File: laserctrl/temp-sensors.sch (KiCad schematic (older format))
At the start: 25 parts, among them P4 CONN_2, P5 CONN_2, P6 CONN_2, P7 CONN_2, Q2 BC807, Q3 BC807

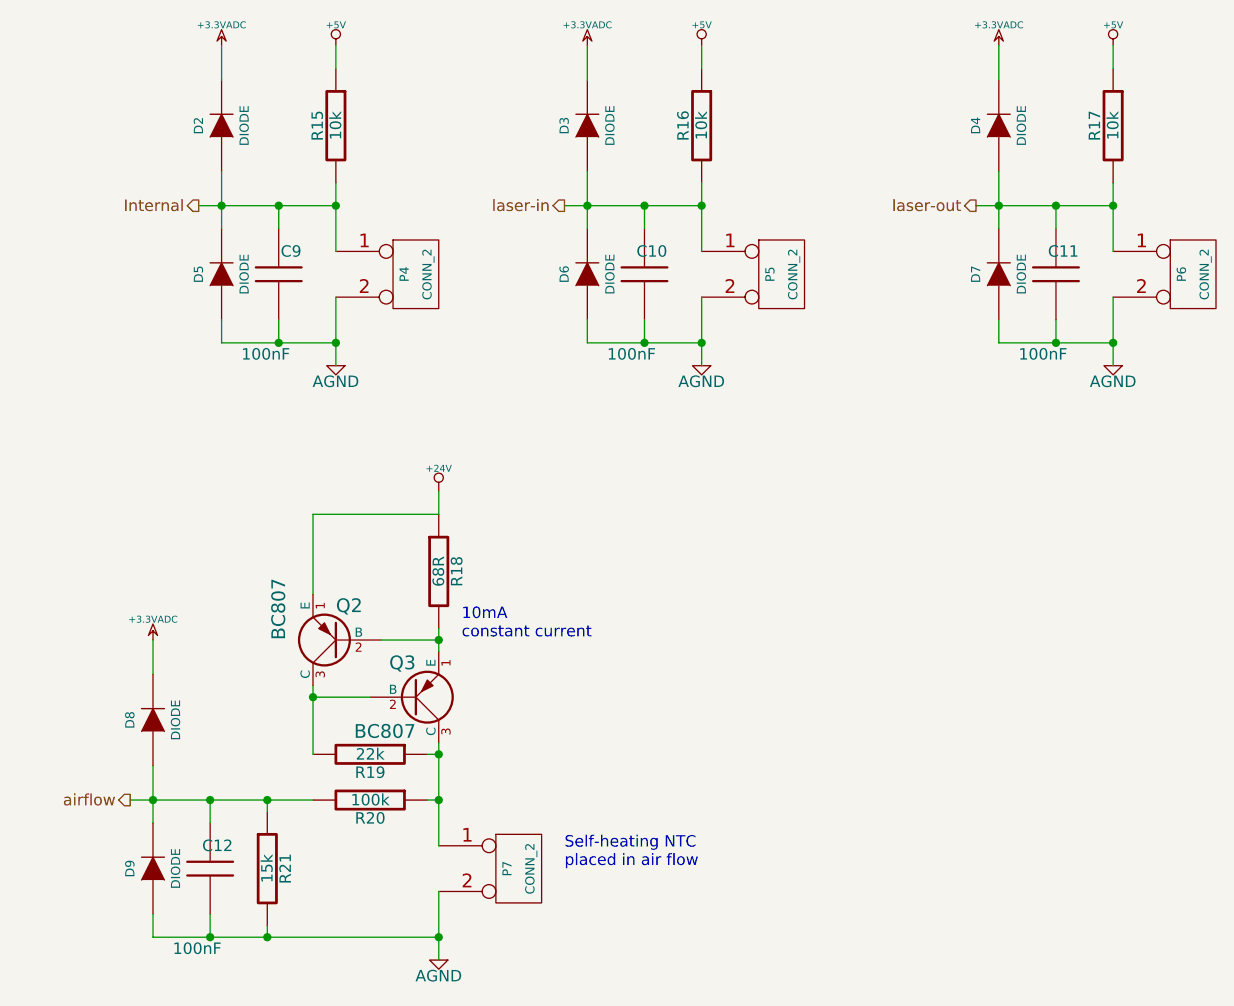
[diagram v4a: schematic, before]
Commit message: Started assigning footprints
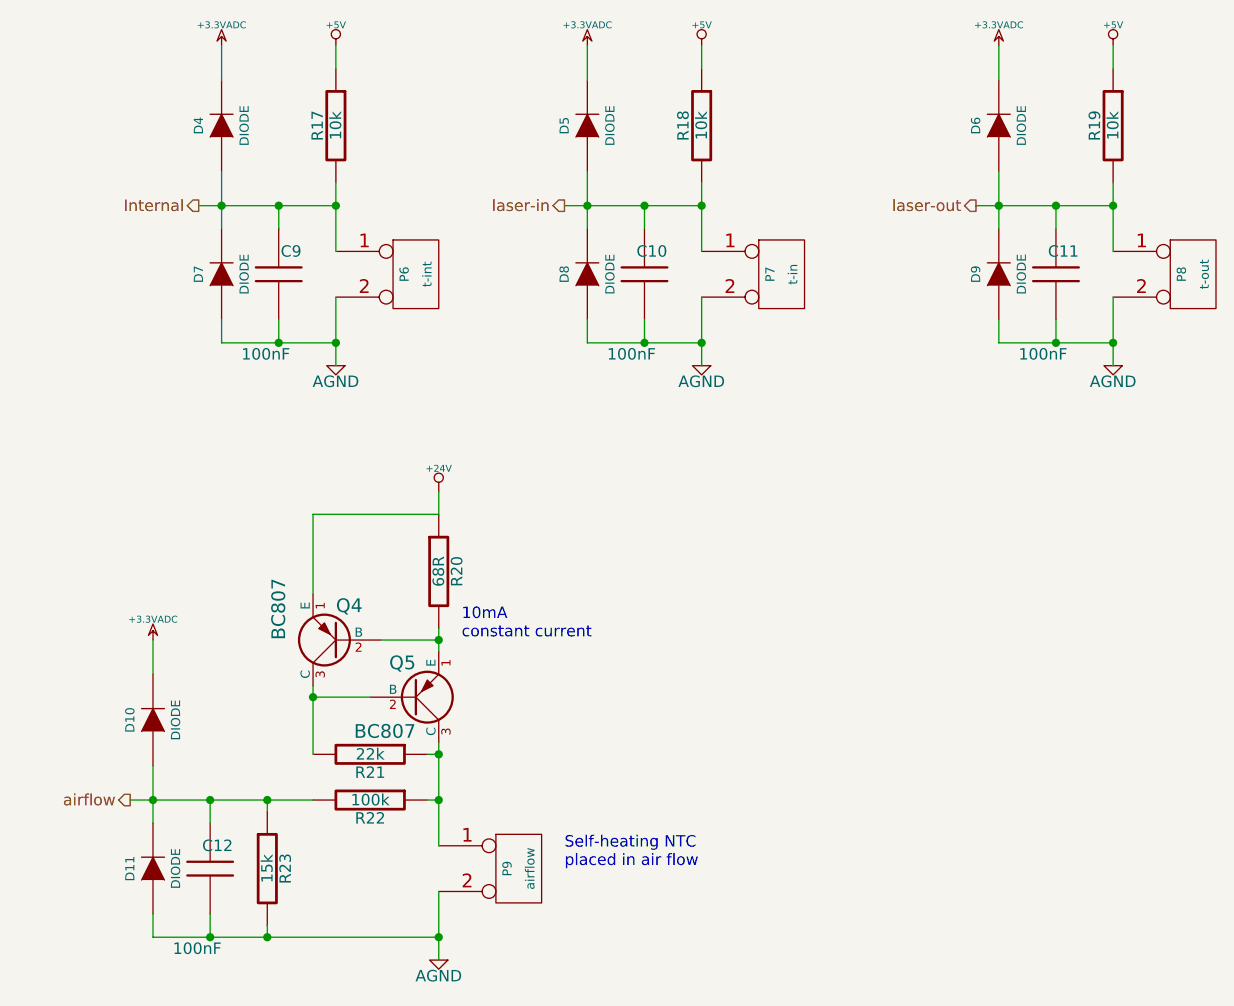
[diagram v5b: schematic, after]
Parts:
- P6: renamed from P4; value CONN_2 -> t-int
- P7: renamed from P5; value CONN_2 -> t-in
- P8: renamed from P6; value CONN_2 -> t-out
- P9: renamed from P7; value CONN_2 -> airflow
- renumbered D8 to D10, D9 to D11, D2 to D4, D3 to D5, D4 to D6, D5 to D7, D6 to D8, D7 to D9, Q2 to Q4, Q3 to Q5, R15 to R17, R16 to R18, R17 to R19, R18 to R20, R19 to R21, R20 to R22, R21 to R23
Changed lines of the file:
@@
-EESchema Schematic File Version 2  date 2011-11-07T21:51:12 CET
+EESchema Schematic File Version 2  date 2011-11-07T23:14:52 CET
 LIBS:power
 LIBS:device
@@
 $Descr A4 11700 8267
 encoding utf-8
-Sheet 4 12
+Sheet 5 12
 Title ""
 Date "7 nov 2011"
@@
 Connection ~ 2000 3950
 $Comp
-L R R19
+L R R21
 U 1 1 4EB5C802
 P 2250 4200
-F 0 "R19" V 2330 4200 50  0000 C CNN
+F 0 "R21" V 2330 4200 50  0000 C CNN
 F 1 "22k" V 2250 4200 50  0000 C CNN
 	1    2250 4200
@@
 10mA\nconstant current
 $Comp
-L +24V #PWR36
+L +24V #PWR031
 U 1 1 4EB542F9
 P 2550 3050
-F 0 "#PWR36" H 2550 3000 20  0001 C CNN
+F 0 "#PWR031" H 2550 3000 20  0001 C CNN
 F 1 "+24V" H 2550 3150 30  0000 C CNN
 	1    2550 3050
@@
 $EndComp
 $Comp
-L R R18
+L R R20
 U 1 1 4EB542D5
 P 2550 3400
-F 0 "R18" V 2630 3400 50  0000 C CNN
+F 0 "R20" V 2630 3400 50  0000 C CNN
 F 1 "68R" V 2550 3400 50  0000 C CNN
 	1    2550 3400
@@
 $EndComp
 $Comp
-L PNP Q2
+L PNP Q4
 U 1 1 4EB542BA
 P 2100 3700
-F 0 "Q2" H 2100 3550 60  0000 R CNN
+F 0 "Q4" H 2100 3550 60  0000 R CNN
 F 1 "BC807" V 2350 3700 60  0000 R CNN
 	1    2100 3700
@@
 $EndComp
 $Comp
-L PNP Q3
+L PNP Q5
 U 1 1 4EB542A8
 P 2450 3950
-F 0 "Q3" H 2450 3800 60  0000 R CNN
+F 0 "Q5" H 2450 3800 60  0000 R CNN
 F 1 "BC807" H 2450 4100 60  0000 R CNN
 	1    2450 3950
@@
 $EndComp
 $Comp
-L R R20
+L R R22
 U 1 1 4EB528F0
 P 2250 4400
-F 0 "R20" V 2330 4400 50  0000 C CNN
+F 0 "R22" V 2330 4400 50  0000 C CNN
 F 1 "100k" V 2250 4400 50  0000 C CNN
 	1    2250 4400
@@
 $EndComp
 $Comp
-L R R21
+L R R23
 U 1 1 4EB528C5
 P 1800 4700
-F 0 "R21" V 1880 4700 50  0000 C CNN
+F 0 "R23" V 1880 4700 50  0000 C CNN
 F 1 "15k" V 1800 4700 50  0000 C CNN
 	1    1800 4700
@@
 $EndComp
 $Comp
-L AGND #PWR38
+L AGND #PWR032
 U 1 1 4EB5260B
 P 2550 5100
-F 0 "#PWR38" H 2550 5100 40  0001 C CNN
+F 0 "#PWR032" H 2550 5100 40  0001 C CNN
 F 1 "AGND" H 2550 5030 50  0000 C CNN
 	1    2550 5100
@@
 airflow
 $Comp
-L CONN_2 P7
+L CONN_2 P9
 U 1 1 4EB5260A
 P 2900 4700
-F 0 "P7" V 2850 4700 40  0000 C CNN
-F 1 "CONN_2" V 2950 4700 40  0000 C CNN
+F 0 "P9" V 2850 4700 40  0000 C CNN
+F 1 "airflow" V 2950 4700 40  0000 C CNN
 	1    2900 4700
 	1    0    0    -1
 $EndComp
 $Comp
-L DIODE D8
+L DIODE D10
 U 1 1 4EB52608
 P 1300 4050
-F 0 "D8" H 1300 4150 40  0000 C CNN
+F 0 "D10" H 1300 4150 40  0000 C CNN
 F 1 "DIODE" H 1300 3950 40  0000 C CNN
 	1    1300 4050
@@
 $EndComp
 $Comp
-L DIODE D9
+L DIODE D11
 U 1 1 4EB52607
 P 1300 4700
-F 0 "D9" H 1300 4800 40  0000 C CNN
+F 0 "D11" H 1300 4800 40  0000 C CNN
 F 1 "DIODE" H 1300 4600 40  0000 C CNN
 	1    1300 4700
@@
 $EndComp
 $Comp
-L +3.3VADC #PWR37
+L +3.3VADC #PWR033
 U 1 1 4EB52606
 P 1300 3700
-F 0 "#PWR37" H 1300 3820 20  0001 C CNN
+F 0 "#PWR033" H 1300 3820 20  0001 C CNN
 F 1 "+3.3VADC" H 1300 3790 30  0000 C CNN
 	1    1300 3700
@@
 $EndComp
 $Comp
-L +3.3VADC #PWR31
+L +3.3VADC #PWR034
 U 1 1 4EB52599
 P 5000 1100
-F 0 "#PWR31" H 5000 1220 20  0001 C CNN
+F 0 "#PWR034" H 5000 1220 20  0001 C CNN
 F 1 "+3.3VADC" H 5000 1190 30  0000 C CNN
 	1    5000 1100
@@
 $EndComp
 $Comp
-L DIODE D7
+L DIODE D9
 U 1 1 4EB52598
 P 5000 2100
-F 0 "D7" H 5000 2200 40  0000 C CNN
+F 0 "D9" H 5000 2200 40  0000 C CNN
 F 1 "DIODE" H 5000 2000 40  0000 C CNN
 	1    5000 2100
@@
 $EndComp
 $Comp
-L DIODE D4
+L DIODE D6
 U 1 1 4EB52597
 P 5000 1450
-F 0 "D4" H 5000 1550 40  0000 C CNN
+F 0 "D6" H 5000 1550 40  0000 C CNN
 F 1 "DIODE" H 5000 1350 40  0000 C CNN
 	1    5000 1450
@@
 $EndComp
 $Comp
-L +5V #PWR32
+L +5V #PWR035
 U 1 1 4EB52596
 P 5500 1100
-F 0 "#PWR32" H 5500 1190 20  0001 C CNN
+F 0 "#PWR035" H 5500 1190 20  0001 C CNN
 F 1 "+5V" H 5500 1190 30  0000 C CNN
 	1    5500 1100
@@
 $EndComp
 $Comp
-L CONN_2 P6
+L CONN_2 P8
 U 1 1 4EB52595
 P 5850 2100
-F 0 "P6" V 5800 2100 40  0000 C CNN
-F 1 "CONN_2" V 5900 2100 40  0000 C CNN
+F 0 "P8" V 5800 2100 40  0000 C CNN
+F 1 "t-out" V 5900 2100 40  0000 C CNN
 	1    5850 2100
 	1    0    0    -1
@@
 laser-out
 $Comp
-L AGND #PWR35
+L AGND #PWR036
 U 1 1 4EB52594
 P 5500 2500
-F 0 "#PWR35" H 5500 2500 40  0001 C CNN
+F 0 "#PWR036" H 5500 2500 40  0001 C CNN
 F 1 "AGND" H 5500 2430 50  0000 C CNN
 	1    5500 2500
@@
 $EndComp
 $Comp
-L R R17
+L R R19
 U 1 1 4EB52592
 P 5500 1450
-F 0 "R17" V 5580 1450 50  0000 C CNN
+F 0 "R19" V 5580 1450 50  0000 C CNN
 F 1 "10k" V 5500 1450 50  0000 C CNN
 	1    5500 1450
@@
 $EndComp
 $Comp
-L R R16
+L R R18
 U 1 1 4EB52540
 P 3700 1450
-F 0 "R16" V 3780 1450 50  0000 C CNN
+F 0 "R18" V 3780 1450 50  0000 C CNN
 F 1 "10k" V 3700 1450 50  0000 C CNN
 	1    3700 1450
@@
 $EndComp
 $Comp
-L AGND #PWR34
+L AGND #PWR037
 U 1 1 4EB5253E
 P 3700 2500
-F 0 "#PWR34" H 3700 2500 40  0001 C CNN
+F 0 "#PWR037" H 3700 2500 40  0001 C CNN
 F 1 "AGND" H 3700 2430 50  0000 C CNN
 	1    3700 2500
@@
 laser-in
 $Comp
-L CONN_2 P5
+L CONN_2 P7
 U 1 1 4EB5253D
 P 4050 2100
-F 0 "P5" V 4000 2100 40  0000 C CNN
-F 1 "CONN_2" V 4100 2100 40  0000 C CNN
+F 0 "P7" V 4000 2100 40  0000 C CNN
+F 1 "t-in" V 4100 2100 40  0000 C CNN
 	1    4050 2100
 	1    0    0    -1
 $EndComp
 $Comp
-L +5V #PWR30
+L +5V #PWR038
 U 1 1 4EB5253C
 P 3700 1100
-F 0 "#PWR30" H 3700 1190 20  0001 C CNN
+F 0 "#PWR038" H 3700 1190 20  0001 C CNN
 F 1 "+5V" H 3700 1190 30  0000 C CNN
 	1    3700 1100
@@
 $EndComp
 $Comp
-L DIODE D3
+L DIODE D5
 U 1 1 4EB5253B
 P 3200 1450
-F 0 "D3" H 3200 1550 40  0000 C CNN
+F 0 "D5" H 3200 1550 40  0000 C CNN
 F 1 "DIODE" H 3200 1350 40  0000 C CNN
 	1    3200 1450
@@
 $EndComp
 $Comp
-L DIODE D6
+L DIODE D8
 U 1 1 4EB5253A
 P 3200 2100
-F 0 "D6" H 3200 2200 40  0000 C CNN
+F 0 "D8" H 3200 2200 40  0000 C CNN
 F 1 "DIODE" H 3200 2000 40  0000 C CNN
 	1    3200 2100
@@
 $EndComp
 $Comp
-L +3.3VADC #PWR29
+L +3.3VADC #PWR039
 U 1 1 4EB52539
 P 3200 1100
-F 0 "#PWR29" H 3200 1220 20  0001 C CNN
+F 0 "#PWR039" H 3200 1220 20  0001 C CNN
 F 1 "+3.3VADC" H 3200 1190 30  0000 C CNN
 	1    3200 1100
@@
 $EndComp
 $Comp
-L +3.3VADC #PWR27
+L +3.3VADC #PWR040
 U 1 1 4EB52427
 P 1600 1100
-F 0 "#PWR27" H 1600 1220 20  0001 C CNN
+F 0 "#PWR040" H 1600 1220 20  0001 C CNN
 F 1 "+3.3VADC" H 1600 1190 30  0000 C CNN
 	1    1600 1100
@@
 $EndComp
 $Comp
-L DIODE D5
+L DIODE D7
 U 1 1 4EB52405
 P 1600 2100
-F 0 "D5" H 1600 2200 40  0000 C CNN
+F 0 "D7" H 1600 2200 40  0000 C CNN
 F 1 "DIODE" H 1600 2000 40  0000 C CNN
 	1    1600 2100
@@
 $EndComp
 $Comp
-L DIODE D2
+L DIODE D4
 U 1 1 4EB523F4
 P 1600 1450
-F 0 "D2" H 1600 1550 40  0000 C CNN
+F 0 "D4" H 1600 1550 40  0000 C CNN
 F 1 "DIODE" H 1600 1350 40  0000 C CNN
 	1    1600 1450
@@
 $EndComp
 $Comp
-L +5V #PWR28
+L +5V #PWR041
 U 1 1 4EB523C5
 P 2100 1100
-F 0 "#PWR28" H 2100 1190 20  0001 C CNN
+F 0 "#PWR041" H 2100 1190 20  0001 C CNN
 F 1 "+5V" H 2100 1190 30  0000 C CNN
 	1    2100 1100
@@
 $EndComp
 $Comp
-L CONN_2 P4
+L CONN_2 P6
 U 1 1 4EB523A3
 P 2450 2100
-F 0 "P4" V 2400 2100 40  0000 C CNN
-F 1 "CONN_2" V 2500 2100 40  0000 C CNN
+F 0 "P6" V 2400 2100 40  0000 C CNN
+F 1 "t-int" V 2500 2100 40  0000 C CNN
 	1    2450 2100
 	1    0    0    -1
@@
 Internal
 $Comp
-L AGND #PWR33
+L AGND #PWR042
 U 1 1 4EB472F1
 P 2100 2500
-F 0 "#PWR33" H 2100 2500 40  0001 C CNN
+F 0 "#PWR042" H 2100 2500 40  0001 C CNN
 F 1 "AGND" H 2100 2430 50  0000 C CNN
 	1    2100 2500
@@
 $EndComp
 $Comp
-L R R15
+L R R17
 U 1 1 4EB46A84
 P 2100 1450
-F 0 "R15" V 2180 1450 50  0000 C CNN
+F 0 "R17" V 2180 1450 50  0000 C CNN
 F 1 "10k" V 2100 1450 50  0000 C CNN
 	1    2100 1450

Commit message: Use double-shottky diodes in stead of tons of discrete miniMELFs
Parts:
- removed D10, D11, D4, D5, D6, D7, D8, D9: DIODE, symbol DIODE
- added D3, D4, D5, D6: BAT 54S, symbol DIODE2
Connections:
- wire segments 50 -> 46
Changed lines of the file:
@@
-EESchema Schematic File Version 2  date 2011-11-09T19:37:00 CET
+EESchema Schematic File Version 2  date 2011-11-09T22:36:32 CET
 LIBS:power
 LIBS:device
@@
 LIBS:microsd
 LIBS:jumper3
+LIBS:diode2
+LIBS:laserctrl-cache
 EELAYER 25  0
 EELAYER END
@@
 Comment4 ""
 $EndDescr
+Wire Wire Line
+	1300 4100 1300 3700
+Wire Wire Line
+	2000 4400 1200 4400
+Connection ~ 1300 4400
+Wire Wire Line
+	5000 2100 5000 2400
+Wire Wire Line
+	5000 2400 5500 2400
+Wire Wire Line
+	4900 1800 5500 1800
+Connection ~ 5000 1800
+Wire Wire Line
+	5000 1500 5000 1100
+Wire Wire Line
+	3200 2100 3200 2400
+Wire Wire Line
+	3200 2400 3700 2400
+Wire Wire Line
+	3100 1800 3700 1800
+Connection ~ 3200 1800
+Wire Wire Line
+	3200 1500 3200 1100
+Wire Wire Line
+	1600 1500 1600 1100
 Connection ~ 2550 4200
 Wire Wire Line
@@
 Wire Wire Line
 	2500 4400 2550 4400
-Wire Wire Line
-	1600 1100 1600 1250
 Connection ~ 1600 1800
 Wire Wire Line
@@
 Connection ~ 2100 2400
 Wire Wire Line
-	1600 2300 1600 2400
-Wire Wire Line
-	1600 2400 2100 2400
+	2100 2400 1600 2400
 Connection ~ 1850 2400
-Wire Wire Line
-	1600 1900 1600 1650
-Wire Wire Line
-	3200 1900 3200 1650
 Connection ~ 3450 2400
-Wire Wire Line
-	3700 2400 3200 2400
-Wire Wire Line
-	3200 2400 3200 2300
 Connection ~ 3700 2400
 Wire Wire Line
@@
 Connection ~ 3700 1800
 Wire Wire Line
-	3100 1800 3700 1800
-Wire Wire Line
 	3450 2400 3450 2300
 Wire Wire Line
@@
 Wire Wire Line
 	3700 1100 3700 1200
-Connection ~ 3200 1800
-Wire Wire Line
-	3200 1100 3200 1250
-Wire Wire Line
-	5000 1100 5000 1250
-Connection ~ 5000 1800
 Wire Wire Line
 	5500 1100 5500 1200
@@
 Wire Wire Line
 	5250 2300 5250 2400
-Wire Wire Line
-	4900 1800 5500 1800
 Connection ~ 5500 1800
 Wire Wire Line
 	5500 2500 5500 2200
 Connection ~ 5500 2400
-Wire Wire Line
-	5000 2300 5000 2400
-Wire Wire Line
-	5000 2400 5500 2400
 Connection ~ 5250 2400
-Wire Wire Line
-	5000 1900 5000 1650
-Wire Wire Line
-	1300 4500 1300 4250
 Connection ~ 1550 5000
-Wire Wire Line
-	1300 4900 1300 5000
 Connection ~ 2550 5000
 Wire Wire Line
@@
 	1550 4400 1550 4500
 Connection ~ 1550 4400
-Connection ~ 1300 4400
-Wire Wire Line
-	1300 3700 1300 3850
-Wire Wire Line
-	1200 4400 2000 4400
-Wire Wire Line
-	1300 5000 2550 5000
+Wire Wire Line
+	2550 5000 1300 5000
 Wire Wire Line
 	2550 3150 2550 3050
@@
 	2000 3900 2000 4200
 Connection ~ 2000 3950
+Wire Wire Line
+	1600 2400 1600 2100
+Wire Wire Line
+	1300 5000 1300 4700
+$Comp
+L DIODE2 D6
+U 1 1 4EBAE319
+P 1300 4400
+F 0 "D6" H 1450 4500 60  0000 C CNN
+F 1 "BAT 54S" H 1550 4600 60  0000 C CNN
+	1    1300 4400
+	-1   0    0    1
+$EndComp
+$Comp
+L +3.3VADC #PWR030
+U 1 1 4EBAE2EF
+P 5000 1100
+F 0 "#PWR030" H 5000 1220 20  0001 C CNN
+F 1 "+3.3VADC" H 5000 1190 30  0000 C CNN
+	1    5000 1100
+	1    0    0    -1
+$EndComp
+$Comp
+L DIODE2 D5
+U 1 1 4EBAE2EE
+P 5000 1800
+F 0 "D5" H 5150 1900 60  0000 C CNN
+F 1 "BAT 54S" H 5250 2000 60  0000 C CNN
+	1    5000 1800
+	-1   0    0    1
+$EndComp
+$Comp
+L +3.3VADC #PWR031
+U 1 1 4EBAE2E3
+P 3200 1100
+F 0 "#PWR031" H 3200 1220 20  0001 C CNN
+F 1 "+3.3VADC" H 3200 1190 30  0000 C CNN
+	1    3200 1100
+	1    0    0    -1
+$EndComp
+$Comp
+L DIODE2 D4
+U 1 1 4EBAE2E2
+P 3200 1800
+F 0 "D4" H 3350 1900 60  0000 C CNN
+F 1 "BAT 54S" H 3450 2000 60  0000 C CNN
+	1    3200 1800
+	-1   0    0    1
+$EndComp
+$Comp
+L DIODE2 D3
+U 1 1 4EBAE288
+P 1600 1800
+F 0 "D3" H 1750 1900 60  0000 C CNN
+F 1 "BAT 54S" H 1850 2000 60  0000 C CNN
+	1    1600 1800
+	-1   0    0    1
+$EndComp
 $Comp
 L R R21
@@
 10mA\nconstant current
 $Comp
-L +24V #PWR39
+L +24V #PWR032
 U 1 1 4EB542F9
 P 2550 3050
-F 0 "#PWR39" H 2550 3000 20  0001 C CNN
+F 0 "#PWR032" H 2550 3000 20  0001 C CNN
 F 1 "+24V" H 2550 3150 30  0000 C CNN
 	1    2550 3050
@@
 $EndComp
 $Comp
-L AGND #PWR41
+L AGND #PWR033
 U 1 1 4EB5260B
 P 2550 5100
-F 0 "#PWR41" H 2550 5100 40  0001 C CNN
+F 0 "#PWR033" H 2550 5100 40  0001 C CNN
 F 1 "AGND" H 2550 5030 50  0000 C CNN
 	1    2550 5100
@@
 $EndComp
 $Comp
-L DIODE D10
-U 1 1 4EB52608
-P 1300 4050
-F 0 "D10" H 1300 4150 40  0000 C CNN
-F 1 "DIODE" H 1300 3950 40  0000 C CNN
-	1    1300 4050
-	0    -1   -1   0
-$EndComp
-$Comp
-L DIODE D11
-U 1 1 4EB52607
-P 1300 4700
-F 0 "D11" H 1300 4800 40  0000 C CNN
-F 1 "DIODE" H 1300 4600 40  0000 C CNN
-	1    1300 4700
-	0    -1   -1   0
-$EndComp
-$Comp
-L +3.3VADC #PWR40
+L +3.3VADC #PWR034
 U 1 1 4EB52606
 P 1300 3700
-F 0 "#PWR40" H 1300 3820 20  0001 C CNN
+F 0 "#PWR034" H 1300 3820 20  0001 C CNN
 F 1 "+3.3VADC" H 1300 3790 30  0000 C CNN
 	1    1300 3700
@@
 $EndComp
 $Comp
-L +3.3VADC #PWR34
-U 1 1 4EB52599
-P 5000 1100
-F 0 "#PWR34" H 5000 1220 20  0001 C CNN
-F 1 "+3.3VADC" H 5000 1190 30  0000 C CNN
-	1    5000 1100
-	1    0    0    -1
-$EndComp
-$Comp
-L DIODE D9
-U 1 1 4EB52598
-P 5000 2100
-F 0 "D9" H 5000 2200 40  0000 C CNN
-F 1 "DIODE" H 5000 2000 40  0000 C CNN
-	1    5000 2100
-	0    -1   -1   0
-$EndComp
-$Comp
-L DIODE D6
-U 1 1 4EB52597
-P 5000 1450
-F 0 "D6" H 5000 1550 40  0000 C CNN
-F 1 "DIODE" H 5000 1350 40  0000 C CNN
-	1    5000 1450
-	0    -1   -1   0
-$EndComp
-$Comp
-L +5V #PWR35
+L +5V #PWR035
 U 1 1 4EB52596
 P 5500 1100
-F 0 "#PWR35" H 5500 1190 20  0001 C CNN
+F 0 "#PWR035" H 5500 1190 20  0001 C CNN
 F 1 "+5V" H 5500 1190 30  0000 C CNN
 	1    5500 1100
@@
 laser-out
 $Comp
-L AGND #PWR38
+L AGND #PWR036
 U 1 1 4EB52594
 P 5500 2500
-F 0 "#PWR38" H 5500 2500 40  0001 C CNN
+F 0 "#PWR036" H 5500 2500 40  0001 C CNN
 F 1 "AGND" H 5500 2430 50  0000 C CNN
 	1    5500 2500
@@
 $EndComp
 $Comp
-L AGND #PWR37
+L AGND #PWR037
 U 1 1 4EB5253E
 P 3700 2500
-F 0 "#PWR37" H 3700 2500 40  0001 C CNN
+F 0 "#PWR037" H 3700 2500 40  0001 C CNN
 F 1 "AGND" H 3700 2430 50  0000 C CNN
 	1    3700 2500
@@
 $EndComp
 $Comp
-L +5V #PWR33
+L +5V #PWR038
 U 1 1 4EB5253C
 P 3700 1100
-F 0 "#PWR33" H 3700 1190 20  0001 C CNN
+F 0 "#PWR038" H 3700 1190 20  0001 C CNN
 F 1 "+5V" H 3700 1190 30  0000 C CNN
 	1    3700 1100
@@
 $EndComp
 $Comp
-L DIODE D5
-U 1 1 4EB5253B
-P 3200 1450
-F 0 "D5" H 3200 1550 40  0000 C CNN
-F 1 "DIODE" H 3200 1350 40  0000 C CNN
-	1    3200 1450
-	0    -1   -1   0
-$EndComp
-$Comp
-L DIODE D8
-U 1 1 4EB5253A
-P 3200 2100
-F 0 "D8" H 3200 2200 40  0000 C CNN
-F 1 "DIODE" H 3200 2000 40  0000 C CNN
-	1    3200 2100
-	0    -1   -1   0
-$EndComp
-$Comp
-L +3.3VADC #PWR32
-U 1 1 4EB52539
-P 3200 1100
-F 0 "#PWR32" H 3200 1220 20  0001 C CNN
-F 1 "+3.3VADC" H 3200 1190 30  0000 C CNN
-	1    3200 1100
-	1    0    0    -1
-$EndComp
-$Comp
-L +3.3VADC #PWR30
+L +3.3VADC #PWR039
 U 1 1 4EB52427
 P 1600 1100
-F 0 "#PWR30" H 1600 1220 20  0001 C CNN
+F 0 "#PWR039" H 1600 1220 20  0001 C CNN
 F 1 "+3.3VADC" H 1600 1190 30  0000 C CNN
 	1    1600 1100
@@
 $EndComp
 $Comp
-L DIODE D7
-U 1 1 4EB52405
-P 1600 2100
-F 0 "D7" H 1600 2200 40  0000 C CNN
-F 1 "DIODE" H 1600 2000 40  0000 C CNN
-	1    1600 2100
-	0    -1   -1   0
-$EndComp
-$Comp
-L DIODE D4
-U 1 1 4EB523F4
-P 1600 1450
-F 0 "D4" H 1600 1550 40  0000 C CNN
-F 1 "DIODE" H 1600 1350 40  0000 C CNN
-	1    1600 1450
-	0    -1   -1   0
-$EndComp
-$Comp
-L +5V #PWR31
+L +5V #PWR040
 U 1 1 4EB523C5
 P 2100 1100
-F 0 "#PWR31" H 2100 1190 20  0001 C CNN
+F 0 "#PWR040" H 2100 1190 20  0001 C CNN
 F 1 "+5V" H 2100 1190 30  0000 C CNN
 	1    2100 1100
@@
 Internal
 $Comp
-L AGND #PWR36
+L AGND #PWR041
 U 1 1 4EB472F1
 P 2100 2500
-F 0 "#PWR36" H 2100 2500 40  0001 C CNN
+F 0 "#PWR041" H 2100 2500 40  0001 C CNN
 F 1 "AGND" H 2100 2430 50  0000 C CNN
 	1    2100 2500
